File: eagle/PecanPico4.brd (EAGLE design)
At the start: 49.9 x 25.7 mm, 108 parts, among them IC2 61201, IC3 SI4463/4, IC4 ATMEGA328P-AU, IC5 UBLOX_MAX-6, IC6 61201, J1 AVR_SPI_PRG_6PTH, U1 EEPROM-I2CSMD, X1 MC-921

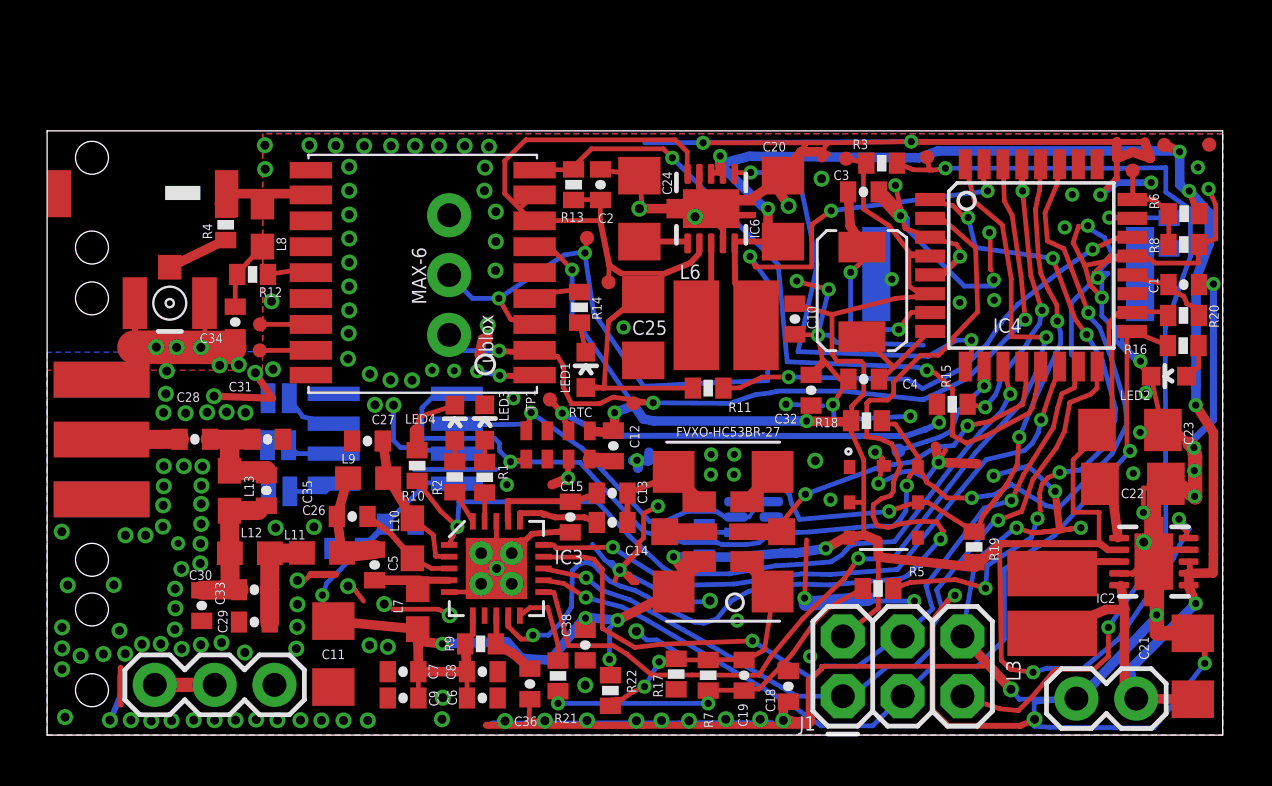
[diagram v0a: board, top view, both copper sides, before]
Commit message: Added breakout for I2C, ADC2/3
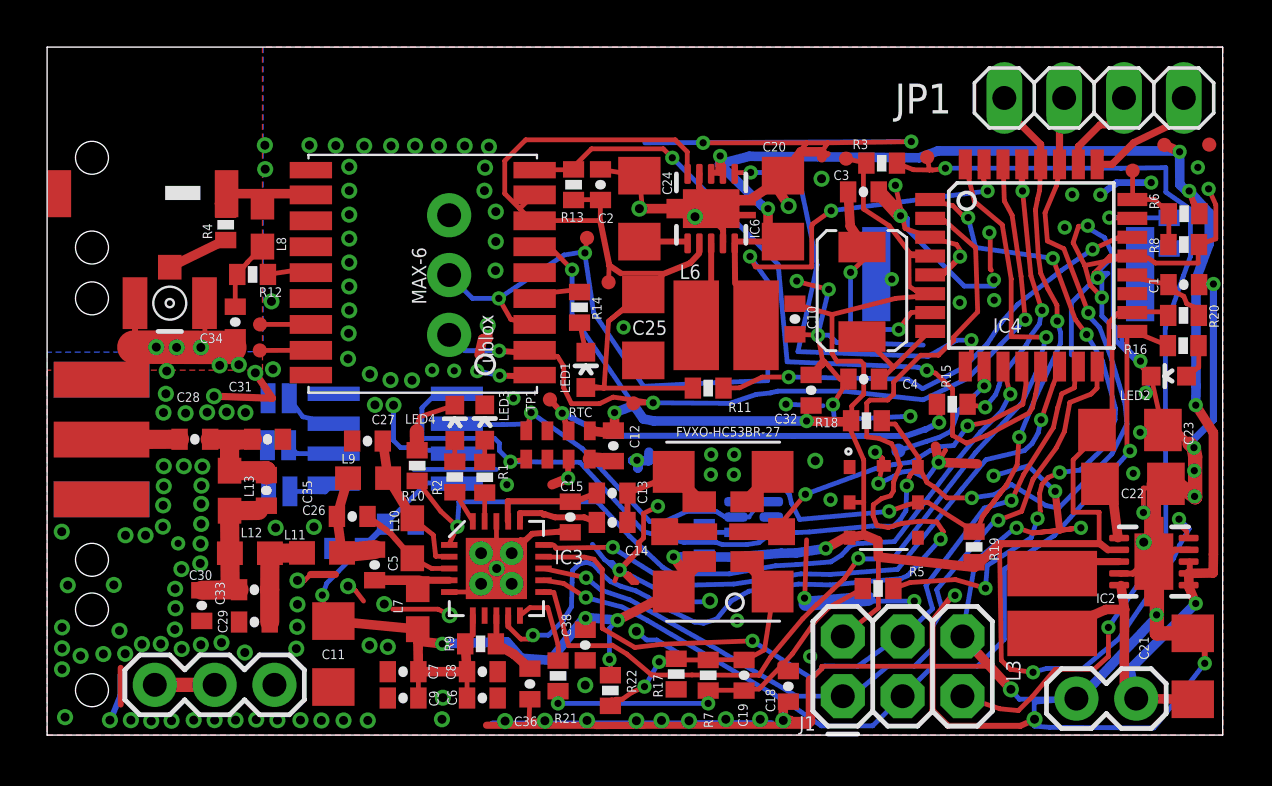
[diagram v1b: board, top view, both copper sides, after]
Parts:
- added JP1: (no value), pinhead:1X04
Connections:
- new net N$18: JP1.1
- new net N$37: JP1.2
- new net N$38: JP1.3
- new net N$39: JP1.4
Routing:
- net GND: track 347.0 -> 331.5 mm
- net ADC2: track 0.00 -> 3.79 mm
- net ADC3: track 0.00 -> 3.24 mm
- net SCL: track 46.5 -> 49.6 mm
- net SDA: track 55.6 -> 58.2 mm
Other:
- board size 49.9 x 25.7 mm -> 49.9 x 29.2 mm
